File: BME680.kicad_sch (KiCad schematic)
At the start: 20 parts, among them IC1 BME680, Q2 BSS138, U2 AP2112K-3.3

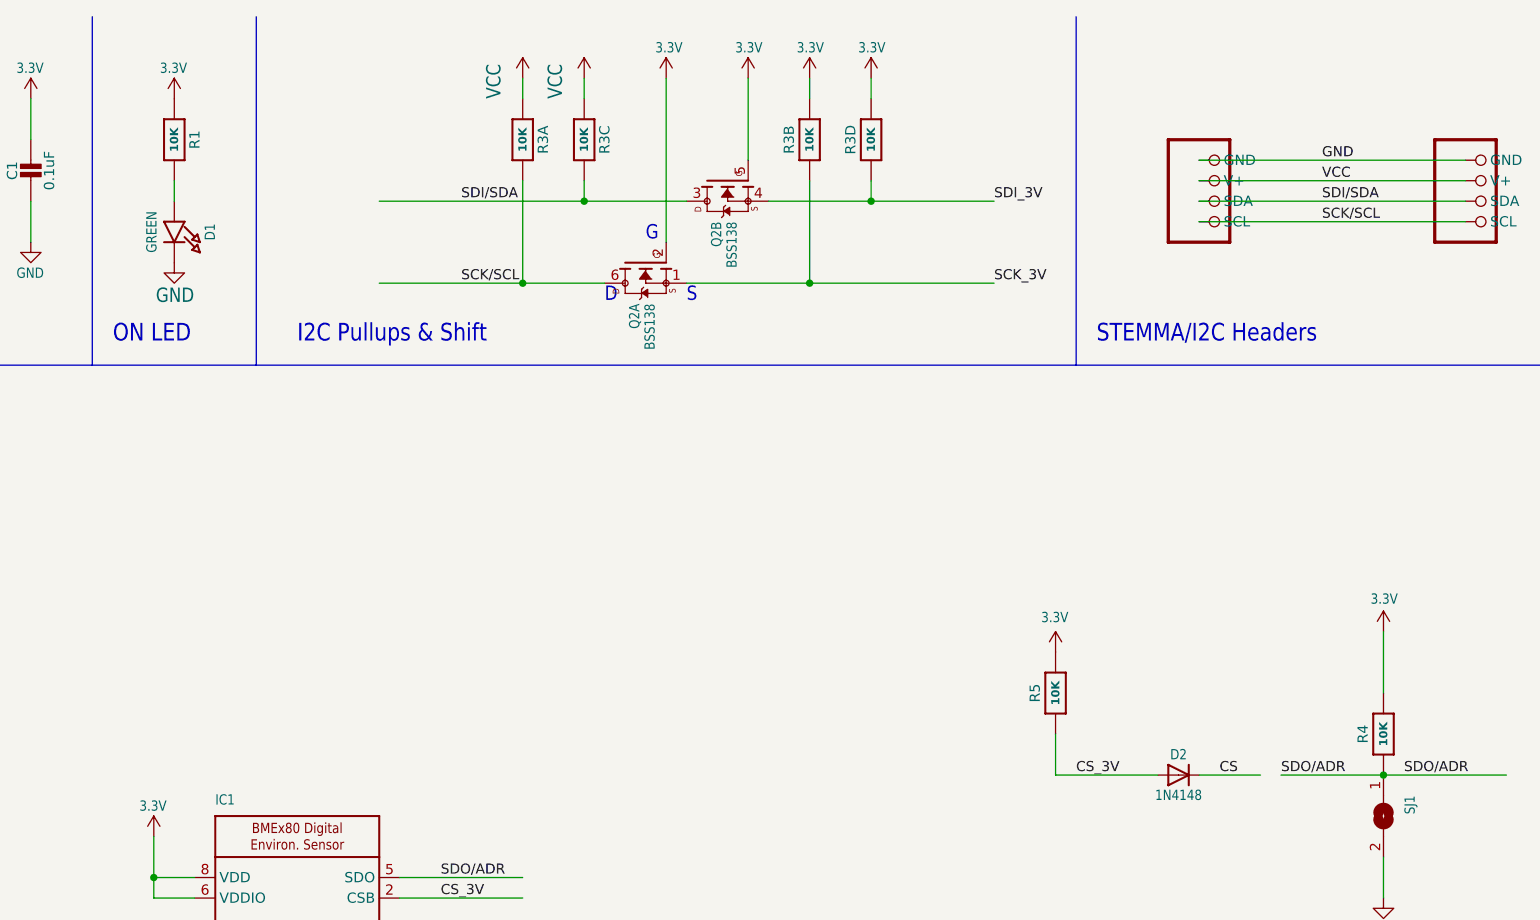
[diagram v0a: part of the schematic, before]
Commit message: updated all resistor libraries
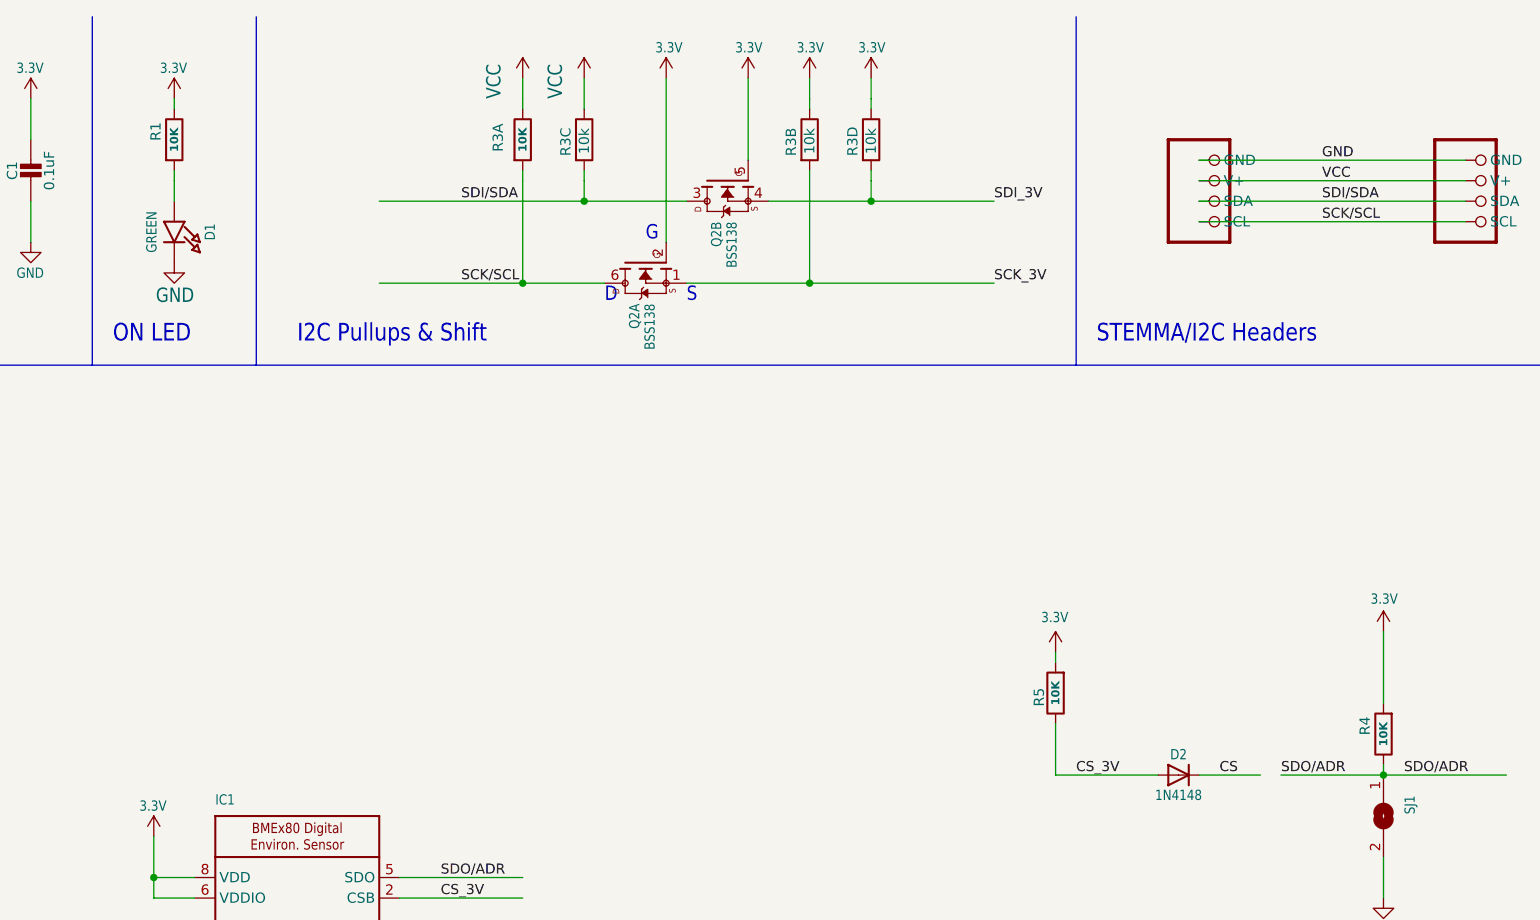
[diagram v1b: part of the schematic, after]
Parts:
- removed unit 3 of R3
- removed unit 4 of R3
- removed unit 2 of R3
- added R3B, R3C, R3D: 10k, symbol Device:R
- R1, R4, R5: symbol BME680-eagle-import:RESISTOR_0603_NOOUT -> Device:R
- R3A: renamed from R3; symbol BME680-eagle-import:RESISTOR_4PACK -> Device:R
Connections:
- net 3.3V: now also R3B.1, R3D.1
- net SCK/SCL: now also R3A.2; no longer R3A.8 (2)
- net SCK_3V: now also R3B.2
- net SDI/SDA: now also R3C.2
- net SDI_3V: now also R3D.2
- net VCC: now also R3C.1

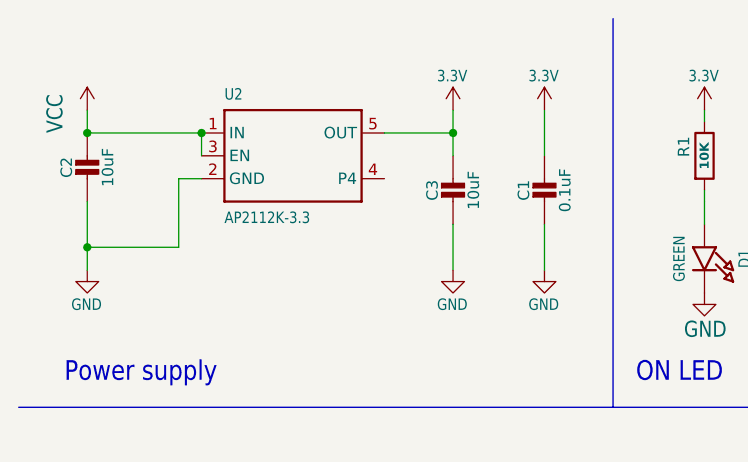
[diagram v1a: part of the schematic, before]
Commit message: updated all capacitor libraries
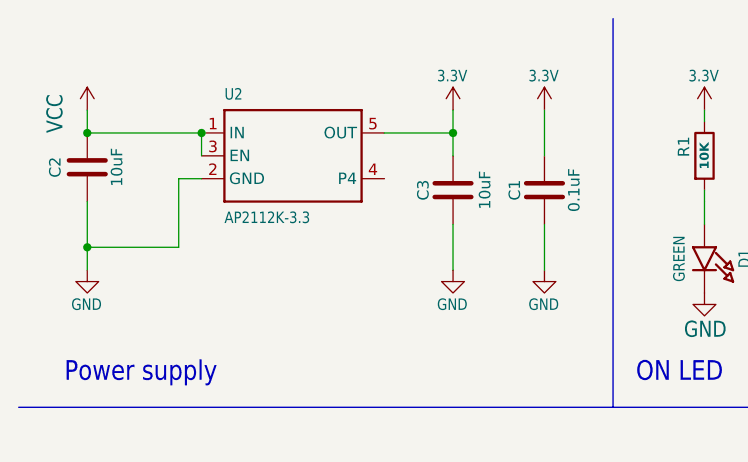
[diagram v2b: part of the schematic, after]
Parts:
- C1: symbol BME680-eagle-import:CAP_CERAMIC0603_NO -> Device:C
- C2, C3: symbol BME680-eagle-import:CAP_CERAMIC0805-NOOUTLINE -> Device:C
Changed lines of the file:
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@@
 	)
 	(symbol
-		(lib_id "BME680-eagle-import:CAP_CERAMIC0805-NOOUTLINE")
-		(at 27.94 40.64 0)
+		(lib_id "Device:C")
+		(at 27.94 39.37 0)
 		(unit 1)
 		(exclude_from_sim no)
@@
 		(dnp no)
 		(property "Reference" "C2"
-			(at 25.65 39.39 90)
+			(at 24.384 39.37 90)
 			(effects
 				(font
@@
 		)
 		(property "Value" "10uF"
-			(at 30.24 39.39 90)
+			(at 31.242 39.37 90)
 			(effects
 				(font
@@
 		)
 		(property "Footprint" "BME680:0805-NO"
-			(at 27.94 40.64 0)
-			(effects
-				(font
-					(size 1.27 1.27)
-				)
-				(hide yes)
-			)
-		)
-		(property "Datasheet" ""
-			(at 27.94 40.64 0)
-			(effects
-				(font
-					(size 1.27 1.27)
-				)
-				(hide yes)
-			)
-		)
-		(property "Description" ""
-			(at 27.94 40.64 0)
+			(at 28.9052 43.18 0)
+			(effects
+				(font
+					(size 1.27 1.27)
+				)
+				(hide yes)
+			)
+		)
+		(property "Datasheet" "~"
+			(at 27.94 39.37 0)
+			(effects
+				(font
+					(size 1.27 1.27)
+				)
+				(hide yes)
+			)
+		)
+		(property "Description" "Unpolarized capacitor"
+			(at 27.94 39.37 0)
 			(effects
 				(font
@@
 	)
 	(symbol
-		(lib_id "BME680-eagle-import:CAP_CERAMIC0805-NOOUTLINE")
-		(at 68.58 43.18 0)
+		(lib_id "Device:C")
+		(at 68.58 41.91 0)
 		(unit 1)
 		(exclude_from_sim no)
@@
 		(dnp no)
 		(property "Reference" "C3"
-			(at 66.29 41.93 90)
+			(at 65.278 41.91 90)
 			(effects
 				(font
@@
 		)
 		(property "Value" "10uF"
-			(at 70.88 41.93 90)
+			(at 72.136 41.91 90)
 			(effects
 				(font
@@
 		)
 		(property "Footprint" "BME680:0805-NO"
-			(at 68.58 43.18 0)
-			(effects
-				(font
-					(size 1.27 1.27)
-				)
-				(hide yes)
-			)
-		)
-		(property "Datasheet" ""
-			(at 68.58 43.18 0)
-			(effects
-				(font
-					(size 1.27 1.27)
-				)
-				(hide yes)
-			)
-		)
-		(property "Description" ""
-			(at 68.58 43.18 0)
+			(at 69.5452 45.72 0)
+			(effects
+				(font
+					(size 1.27 1.27)
+				)
+				(hide yes)
+			)
+		)
+		(property "Datasheet" "~"
+			(at 68.58 41.91 0)
+			(effects
+				(font
+					(size 1.27 1.27)
+				)
+				(hide yes)
+			)
+		)
+		(property "Description" "Unpolarized capacitor"
+			(at 68.58 41.91 0)
 			(effects
 				(font
@@
 	)
 	(symbol
-		(lib_id "BME680-eagle-import:CAP_CERAMIC0603_NO")
-		(at 78.74 43.18 0)
+		(lib_id "Device:C")
+		(at 78.74 41.91 0)
 		(unit 1)
 		(exclude_from_sim no)
@@
 		(dnp no)
 		(property "Reference" "C1"
-			(at 76.45 41.93 90)
+			(at 75.438 41.91 90)
 			(effects
 				(font
@@
 		)
 		(property "Value" "0.1uF"
-			(at 81.04 41.93 90)
+			(at 82.042 41.91 90)
 			(effects
 				(font
@@
 		)
 		(property "Footprint" "BME680:0603-NO"
-			(at 78.74 43.18 0)
-			(effects
-				(font
-					(size 1.27 1.27)
-				)
-				(hide yes)
-			)
-		)
-		(property "Datasheet" ""
-			(at 78.74 43.18 0)
-			(effects
-				(font
-					(size 1.27 1.27)
-				)
-				(hide yes)
-			)
-		)
-		(property "Description" ""
-			(at 78.74 43.18 0)
-			(effects
-				(font
+			(at 79.7052 45.72 0)
+			(effects
+				(font
+					(size 1.27 1.27)
+				)
+				(hide yes)
+			)
+		)
+		(property "Datasheet" "~"
+			(at 78.74 41.91 0)
+			(effects
+				(font
+					(size 1.27 1.27)
+				)
+				(hide yes)
+			)
+		)
+		(property "Description" "Unpolarized capacitor"
+			(at 78.74 41.91 0)
+			(effects
+				(font

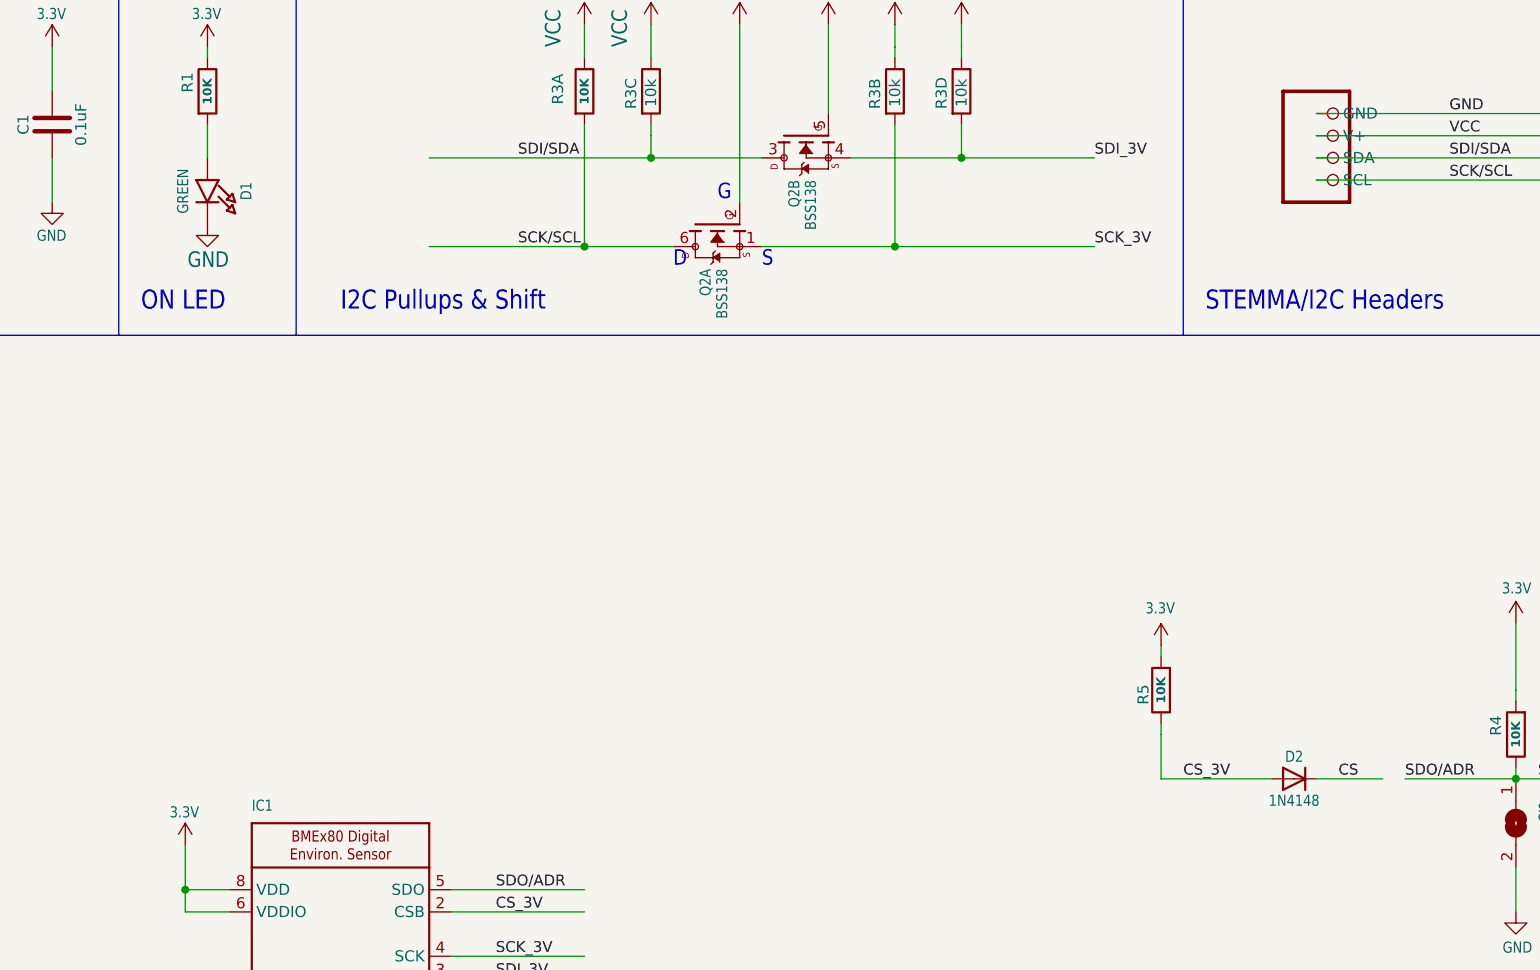
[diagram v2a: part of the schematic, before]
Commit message: updated all diode libraries
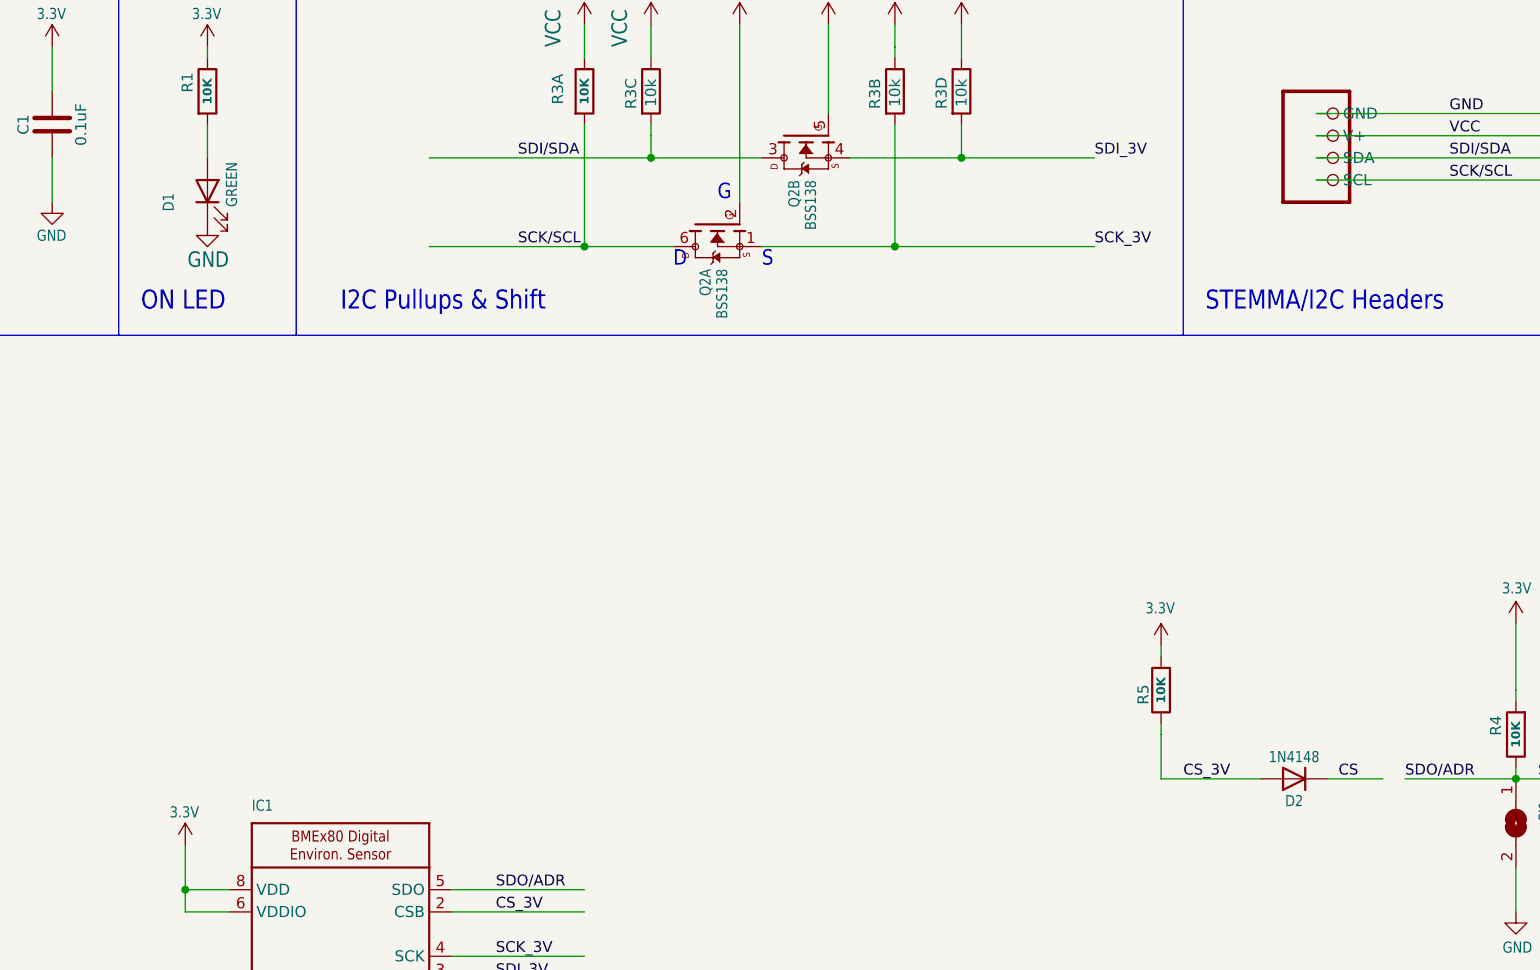
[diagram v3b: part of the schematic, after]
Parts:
- D1: symbol BME680-eagle-import:LED0603_NOOUTLINE -> Device:LED
- D2: symbol BME680-eagle-import:DIODESOD-323 -> Device:D
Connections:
- net CS: now also D2.1 (K); no longer D2.C
- net CS_3V: now also D2.2 (A); no longer D2.A
- net GND: now also D1.1 (K); no longer D1.C
- net at R1.2: now also D1.2 (A); no longer D1.A
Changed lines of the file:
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@@
 		)
 	)
+	(wire
+		(pts
+			(xy 224.79 116.84) (xy 231.14 116.84)
+		)
+		(stroke
+			(width 0.1524)
+			(type solid)
+		)
+	)
 	(polyline
 		(pts
@@
 	(wire
 		(pts
-			(xy 218.44 116.84) (xy 205.74 116.84)
-		)
-		(stroke
-			(width 0.1524)
-			(type solid)
-		)
-	)
-	(wire
-		(pts
 			(xy 182.88 45.72) (xy 198.12 45.72)
 		)
@@
 	(wire
 		(pts
-			(xy 40.64 40.64) (xy 38.1 40.64)
+			(xy 217.17 116.84) (xy 205.74 116.84)
 		)
 		(stroke
@@
 	(wire
 		(pts
-			(xy 96.52 33.02) (xy 96.52 34.29)
+			(xy 40.64 40.64) (xy 38.1 40.64)
 		)
 		(stroke
-			(width 0)
-			(type default)
+			(width 0.1524)
+			(type solid)
 		)
 	)
 	(wire
 		(pts
-			(xy 160.02 55.88) (xy 175.26 55.88)
+			(xy 96.52 33.02) (xy 96.52 34.29)
 		)
 		(stroke
-			(width 0.1524)
-			(type solid)
+			(width 0)
+			(type default)
 		)
 	)
 	(wire
 		(pts
-			(xy 27.94 48.26) (xy 27.94 43.18)
+			(xy 160.02 55.88) (xy 175.26 55.88)
 		)
 		(stroke
@@
 	(wire
 		(pts
-			(xy 223.52 116.84) (xy 231.14 116.84)
+			(xy 27.94 48.26) (xy 27.94 43.18)
 		)
 		(stroke
@@
 	)
 	(symbol
-		(lib_id "BME680-eagle-import:DIODESOD-323")
-		(at 220.98 116.84 0)
+		(lib_id "Device:D")
+		(at 220.98 116.84 180)
 		(unit 1)
 		(exclude_from_sim no)
@@
 		(dnp no)
 		(property "Reference" "D2"
-			(at 220.98 114.3 0)
+			(at 220.98 119.38 0)
 			(effects
 				(font
@@
 		)
 		(property "Value" "1N4148"
-			(at 220.98 119.34 0)
+			(at 220.98 114.34 0)
 			(effects
 				(font
@@
 			)
 		)
-		(property "Datasheet" ""
+		(property "Datasheet" "~"
 			(at 220.98 116.84 0)
 			(effects
@@
 			)
 		)
-		(property "Description" ""
+		(property "Description" "Diode"
 			(at 220.98 116.84 0)
 			(effects
@@
 			)
 		)
-		(pin "A"
+		(property "Sim.Device" "D"
+			(at 220.98 116.84 0)
+			(effects
+				(font
+					(size 1.27 1.27)
+				)
+				(hide yes)
+			)
 		)
-		(pin "C"
+		(property "Sim.Pins" "1=K 2=A"
+			(at 220.98 116.84 0)
+			(effects
+				(font
+					(size 1.27 1.27)
+				)
+				(hide yes)
+			)
+		)
+		(pin "1"
+		)
+		(pin "2"
 		)
 		(instances
@@
 	)
 	(symbol
-		(lib_id "BME680-eagle-import:LED0603_NOOUTLINE")
-		(at 96.52 50.8 270)
+		(lib_id "Device:LED")
+		(at 96.52 49.53 90)
 		(unit 1)
 		(exclude_from_sim no)
@@
 		(dnp no)
 		(property "Reference" "D1"
-			(at 100.965 49.53 0)
+			(at 92.075 50.8 0)
 			(effects
 				(font
@@
 		)
 		(property "Value" "GREEN"
-			(at 93.726 49.53 0)
+			(at 99.314 48.768 0)
 			(effects
 				(font
@@
 		)
 		(property "Footprint" "BME680:CHIPLED_0603_NOOUTLINE"
-			(at 96.52 50.8 0)
+			(at 96.52 49.53 0)
 			(effects
 				(font
@@
 			)
 		)
-		(property "Datasheet" ""
-			(at 96.52 50.8 0)
+		(property "Datasheet" "~"
+			(at 96.52 49.53 0)
 			(effects
 				(font
@@
 			)
 		)
-		(property "Description" ""
-			(at 96.52 50.8 0)
+		(property "Description" "Light emitting diode"
+			(at 96.52 49.53 0)
 			(effects
 				(font
@@
 			)
 		)
-		(pin "C"
+		(pin "2"
 		)
-		(pin "A"
+		(pin "1"
 		)
 		(instances

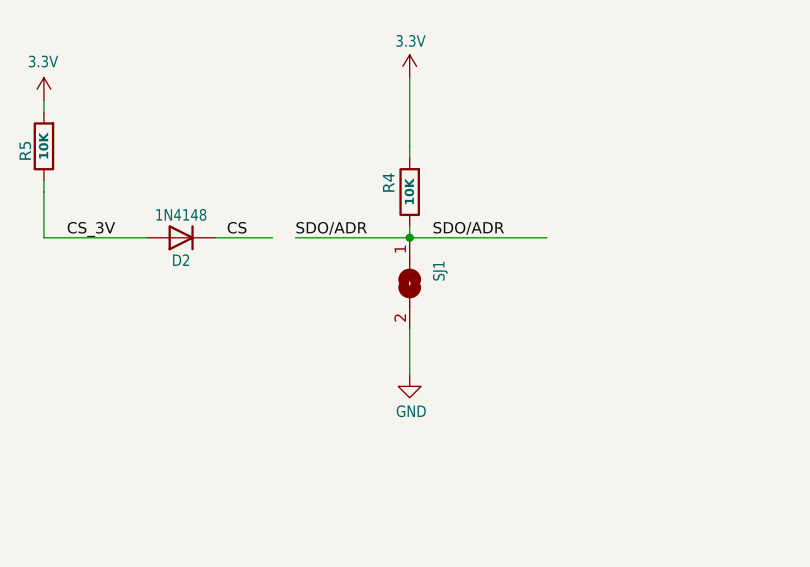
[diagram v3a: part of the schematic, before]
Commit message: updated all solder jumper libraries
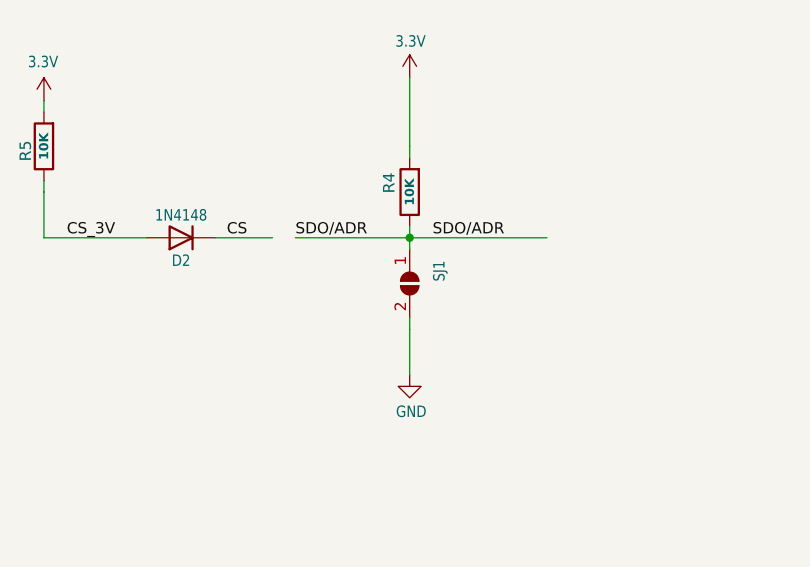
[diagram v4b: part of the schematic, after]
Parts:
- SJ1: symbol BME680-eagle-import:SOLDERJUMPER -> Jumper:SolderJumper_2_Open
